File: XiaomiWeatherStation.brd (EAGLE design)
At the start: 60 x 100 mm, 12 parts, among them J1 1X2-3.5MM, K1 RELAY-SPDT, Q1 BD437

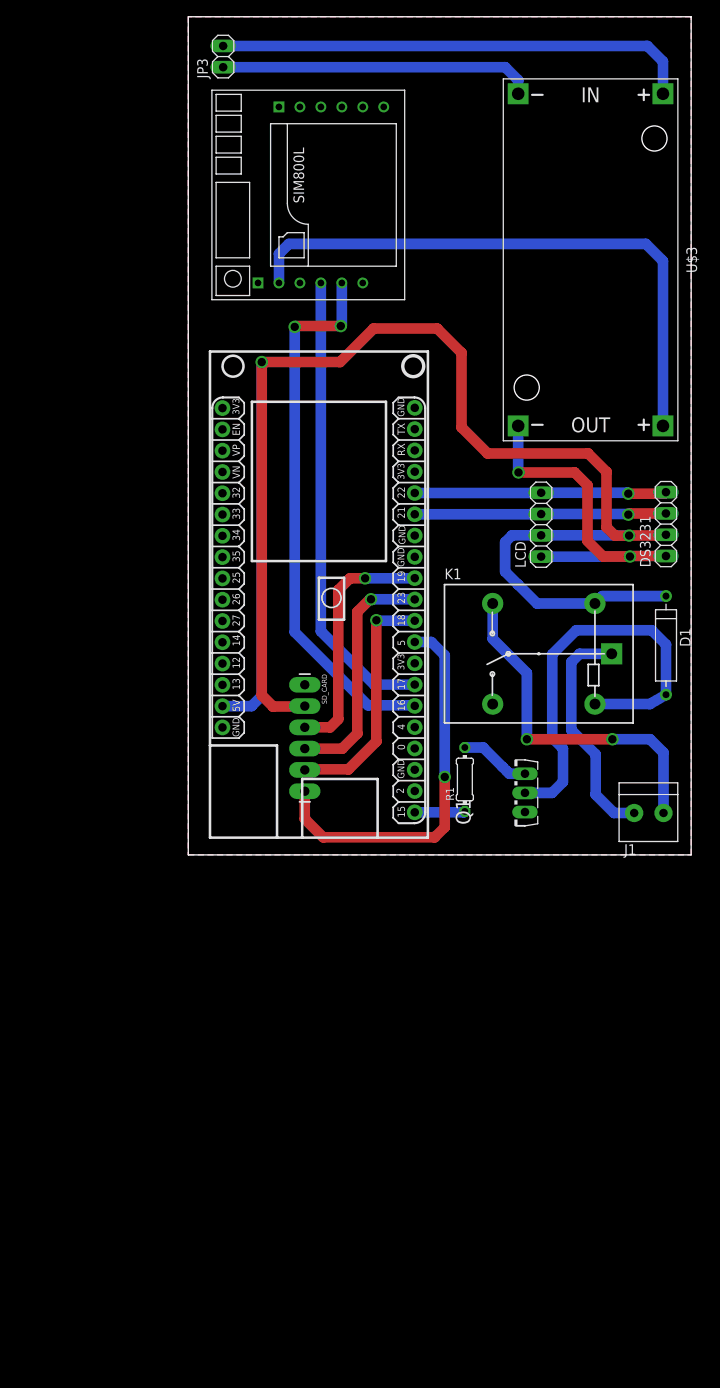
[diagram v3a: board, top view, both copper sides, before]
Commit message: Adds actual sd and ds3231 components in place of header pins
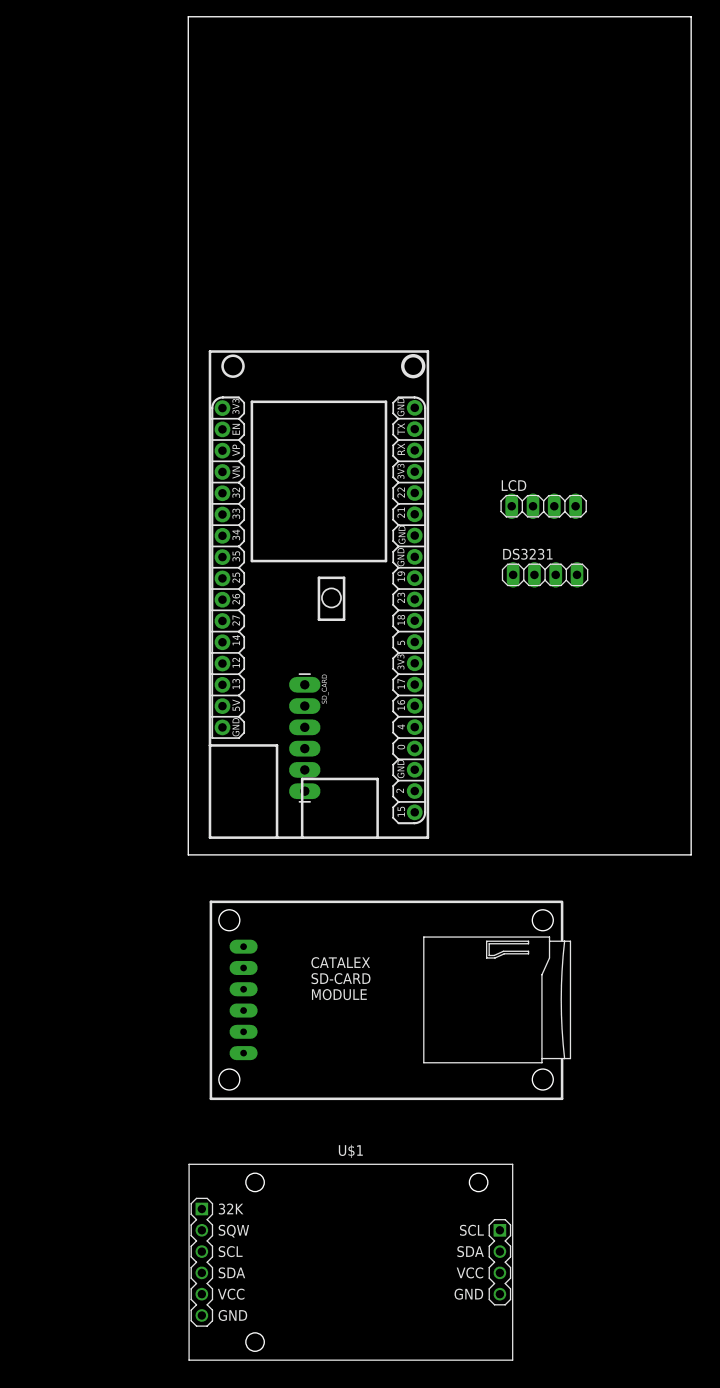
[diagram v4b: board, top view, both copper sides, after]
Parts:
- removed D1: 1N4004IN4004, diode:DIOAD1176W63L850D250B
- removed J1: 1X2-3.5MM, adafruit:1X2-3.5MM
- removed JP3: (no value), pinhead:1X02
- removed K1: RELAY-SPDT, SparkFun-Electromechanical:RELAY_G5LE
- removed Q1: BD437, transistor-power:TO126AV
- removed R1: 1k, rcl:0204/7
- removed U$3: DC-DC-STEP-DOWN-LM2596, diy-modules:DC-DC-STEP-DOWN-LM2596
- added MOD1: CARD-SD-ADAPTER-CATALEX, SD-Card-Module_CATALEX:CARD-SD-ADAPTER-CATALEX
- U$1: value SIM800LMODULE -> RTC-DS3231-AT24C32; device SIM800LMODULE:SIM800LMODULE -> diy-modules:RTC-DS3231-AT24C32
- moved U$1 127.4 mm to (19.4, -48.6), turned to 0 degrees
- moved DS3231 15.6 mm to (42.6, 33.4), turned to 0 degrees
- moved LCD 2.22 mm to (42.4, 41.6), turned to 0 degrees
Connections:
- removed net 3V7: U$1.VCC, U$3.OUT+
- removed net BASE: Q1.B, R1.2
- removed net COLLECTOR: D1.2, K1.5, Q1.C
- removed net IN+: JP3.2, U$3.IN+
- removed net IN-: JP3.1, U$3.IN-
- removed net RELAY: IC1.15, R1.1
- removed net REL_COM: J1.1, K1.1
- removed net REL_NO: J1.2, K1.3
- new net GND.1: U$1.J1.6
- new net VCC.1: U$1.J1.5
- net 5V: now also MOD1.VCC5V, U$1.J2.3; no longer D1.1, K1.2
- net GND: now also MOD1.GND, U$1.J2.4; no longer Q1.E, U$1.GND, U$3.OUT-
- net MISO: now also MOD1.MISO
- net MOSI: now also MOD1.MOSI
- net RXD2: no longer U$1.TX
- net SCK: now also MOD1.SCK
- net SCL: now also U$1.J2.1
- net SDA: now also U$1.J2.2
- net SS: now also MOD1.CS
- net TXD2: no longer U$1.RX
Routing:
- net 5V: track 199.5 -> 0.00 mm, vias 2 -> 0
- net 3V7: track 70.3 -> 0.00 mm
- net RXD2: track 65.1 -> 0.00 mm, vias 2 -> 0
- net IN+: track 57.1 -> 0.00 mm
- net TXD2: track 55.4 -> 0.00 mm
- net COLLECTOR: track 51.1 -> 0.00 mm
- net SS: track 46.2 -> 0.00 mm, vias 1 -> 0
- net REL_NO: track 42.0 -> 0.00 mm, vias 2 -> 0
- net GND: track 41.8 -> 0.00 mm, vias 2 -> 0
- net IN-: track 37.5 -> 0.00 mm
- net SCL: track 30.1 -> 0.00 mm, vias 1 -> 0
- net SDA: track 30.1 -> 0.00 mm, vias 1 -> 0
- net MISO: track 29.5 -> 0.00 mm, vias 1 -> 0
- net MOSI: track 29.0 -> 0.00 mm, vias 1 -> 0
- net SCK: track 29.0 -> 0.00 mm, vias 1 -> 0
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- removed copper zone on layer 1, net GND
- removed copper zone on layer 16, net GND

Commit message: Completes design
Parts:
- removed DS3231: (no value), pinhead:1X04
- removed SD_CARD: (no value), SparkFun-Connectors:1X06_LONGPADS
- moved U$1 82.9 mm to (47.3, 29.5), turned to 90 degrees
- moved MOD1 46.0 mm to (23.4, 28.7), flipped to the bottom
- moved LCD 18.8 mm to (47.4, 59.7), turned to 180 degrees
- moved IC1 4.47 mm to (19.6, 37.6)
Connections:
- net 5V: no longer DS3231.2, SD_CARD.2
- net GND: no longer DS3231.1, SD_CARD.1
- net MISO: no longer SD_CARD.3
- net MOSI: no longer SD_CARD.4
- net SCK: no longer SD_CARD.5
- net SCL: no longer DS3231.4
- net SDA: no longer DS3231.3
- net SS: no longer SD_CARD.6
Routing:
- net 5V: track 0.00 -> 115.5 mm
- net SDA: track 0.00 -> 32.4 mm
- net SCL: track 0.00 -> 25.8 mm
- net GND: track 0.00 -> 21.1 mm
- net SS: track 0.00 -> 13.2 mm
- net MOSI: track 0.00 -> 12.7 mm
- net MISO: track 0.00 -> 12.6 mm
- net SCK: track 0.00 -> 12.5 mm
- added copper zone on layer 1, net GND
- added copper zone on layer 16, net GND
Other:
- board size 60 x 100 mm -> 60 x 66 mm
